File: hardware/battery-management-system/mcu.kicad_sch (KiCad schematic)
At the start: 32 parts, among them J6 ARM-JTAG-SWD, Q5 DMN3404L, Q6 DMN3404L, Q7 DMN3404L, U7 STM32L071CZTx, U8 AT24C512C, U9 NCT75DR2G

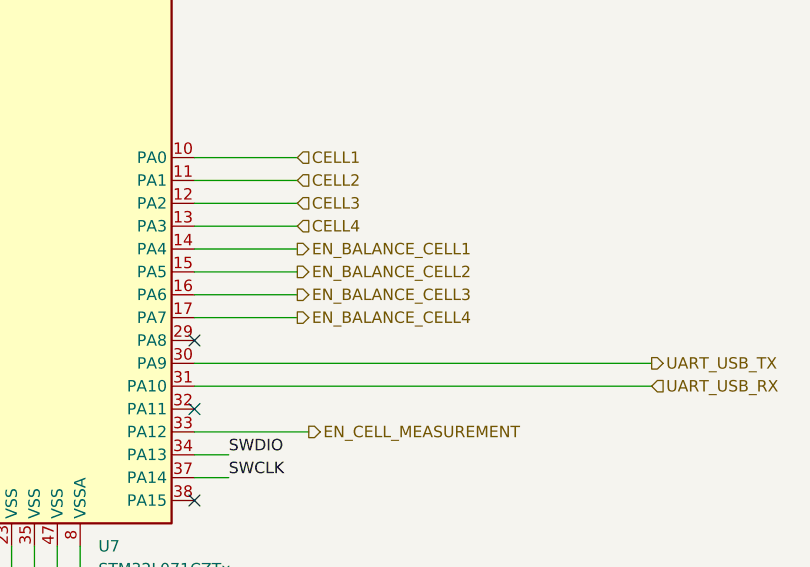
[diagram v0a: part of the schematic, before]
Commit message: finish layout of BMS
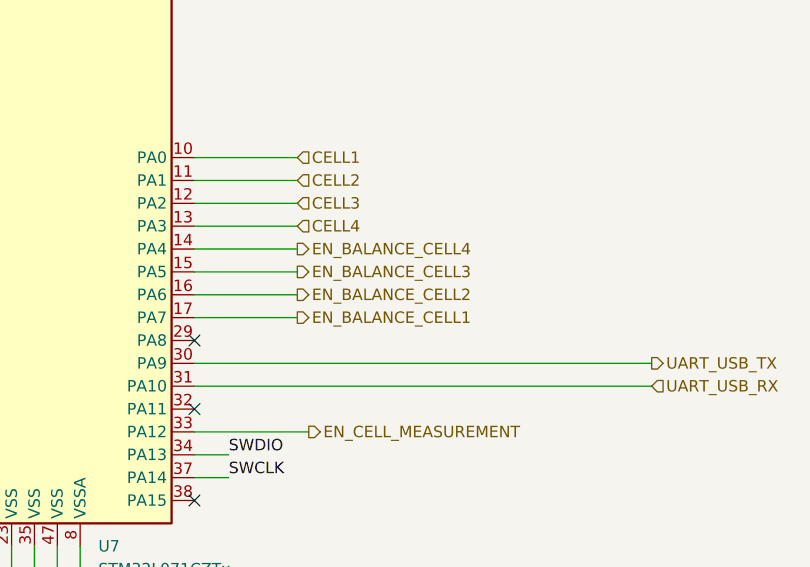
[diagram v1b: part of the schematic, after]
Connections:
- net EN_BALANCE_CELL1: now also U7.17 (PA7); no longer U7.14 (PA4)
- net EN_BALANCE_CELL2: now also U7.16 (PA6); no longer U7.15 (PA5)
- net EN_BALANCE_CELL3: now also U7.15 (PA5); no longer U7.16 (PA6)
- net EN_BALANCE_CELL4: now also U7.14 (PA4); no longer U7.17 (PA7)

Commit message: update symbols from library
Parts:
- C22: Mouser Part Number (none) -> 187-CL31A106MBHNNNE
- C23, C24, C25, C26, C27, C29, C30, C31: Mouser Part Number (none) -> 581-KGM15BR71H104KM
- C28: Mouser Part Number (none) -> 963-UMK107BJ105KA-T
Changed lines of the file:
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@@
 			)
 		)
+		(property "Mouser Part Number" "963-UMK107BJ105KA-T"
+			(at 147.066 39.37 0)
+			(effects
+				(font
+					(size 1.27 1.27)
+				)
+				(hide yes)
+			)
+		)
 		(pin "1"
 		)
@@
 			)
 		)
+		(property "Mouser Part Number" "581-KGM15BR71H104KM"
+			(at 114.046 88.9 0)
+			(effects
+				(font
+					(size 1.27 1.27)
+				)
+				(hide yes)
+			)
+		)
 		(pin "1"
 		)
@@
 			)
 		)
+		(property "Mouser Part Number" "581-KGM15BR71H104KM"
+			(at 82.296 39.37 0)
+			(effects
+				(font
+					(size 1.27 1.27)
+				)
+				(hide yes)
+			)
+		)
 		(pin "1"
 		)
@@
 			)
 		)
+		(property "Mouser Part Number" "581-KGM15BR71H104KM"
+			(at 107.696 39.37 0)
+			(effects
+				(font
+					(size 1.27 1.27)
+				)
+				(hide yes)
+			)
+		)
 		(pin "1"
 		)
@@
 			)
 		)
+		(property "Mouser Part Number" "581-KGM15BR71H104KM"
+			(at 94.996 39.37 0)
+			(effects
+				(font
+					(size 1.27 1.27)
+				)
+				(hide yes)
+			)
+		)
 		(pin "1"
 		)
@@
 			)
 		)
+		(property "Mouser Part Number" "581-KGM15BR71H104KM"
+			(at 134.366 39.37 0)
+			(effects
+				(font
+					(size 1.27 1.27)
+				)
+				(hide yes)
+			)
+		)
 		(pin "1"
 		)
@@
 			)
 		)
+		(property "Mouser Part Number" "581-KGM15BR71H104KM"
+			(at 92.456 121.92 0)
+			(effects
+				(font
+					(size 1.27 1.27)
+				)
+				(hide yes)
+			)
+		)
 		(pin "1"
 		)
@@
 			)
 		)
+		(property "Mouser Part Number" "581-KGM15BR71H104KM"
+			(at 48.006 120.65 0)
+			(effects
+				(font
+					(size 1.27 1.27)
+				)
+				(hide yes)
+			)
+		)
 		(pin "1"
 		)
@@
 			)
 		)
+		(property "Mouser Part Number" "187-CL31A106MBHNNNE"
+			(at 70.866 39.37 0)
+			(effects
+				(font
+					(size 1.27 1.27)
+				)
+				(hide yes)
+			)
+		)
 		(pin "1"
 		)
@@
 			(at 120.396 39.37 0)
 			(effects
+				(font
+					(size 1.27 1.27)
+				)
+				(hide yes)
+			)
+		)
+		(property "Mouser Part Number" "581-KGM15BR71H104KM"
+			(at 120.396 39.37 0)
+			(effects

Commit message: update symbols from library
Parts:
- R23, R24, R30, R31, R32: Mouser Part Number (none) -> 652-CR0603FX-1002ELF
- R25, R26: Mouser Part Number (none) -> 652-CR0603FX-4701ELF
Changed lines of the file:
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@@
+			)
+		)
+		(property "Mouser Part Number" "652-CR0603FX-1002ELF"
+			(at 99.06 168.91 0)
+			(effects
+				(font
+					(size 1.27 1.27)
+				)
+				(hide yes)
 			)
 		)
@@
 			)
 		)
+		(property "Mouser Part Number" "652-CR0603FX-1002ELF"
+			(at 176.53 60.96 0)
+			(effects
+				(font
+					(size 1.27 1.27)
+				)
+				(hide yes)
+			)
+		)
 		(pin "1"
 		)
@@
 			)
 		)
+		(property "Mouser Part Number" "652-CR0603FX-4701ELF"
+			(at 118.11 73.66 0)
+			(effects
+				(font
+					(size 1.27 1.27)
+				)
+				(hide yes)
+			)
+		)
 		(pin "1"
 		)
@@
 			)
 		)
+		(property "Mouser Part Number" "652-CR0603FX-1002ELF"
+			(at 63.5 168.91 0)
+			(effects
+				(font
+					(size 1.27 1.27)
+				)
+				(hide yes)
+			)
+		)
 		(pin "1"
 		)
@@
 			)
 		)
+		(property "Mouser Part Number" "652-CR0603FX-1002ELF"
+			(at 26.67 168.91 0)
+			(effects
+				(font
+					(size 1.27 1.27)
+				)
+				(hide yes)
+			)
+		)
 		(pin "1"
 		)
@@
 		)
 		(property "RS order number" "901-3581"
+			(at 130.81 73.66 0)
+			(effects
+				(font
+					(size 1.27 1.27)
+				)
+				(hide yes)
+			)
+		)
+		(property "Mouser Part Number" "652-CR0603FX-4701ELF"
 			(at 130.81 73.66 0)
 			(effects
@@
 			(at 62.23 68.58 0)
 			(effects
+				(font
+					(size 1.27 1.27)
+				)
+				(hide yes)
+			)
+		)
+		(property "Mouser Part Number" "652-CR0603FX-1002ELF"
+			(at 62.23 68.58 0)
+			(effects

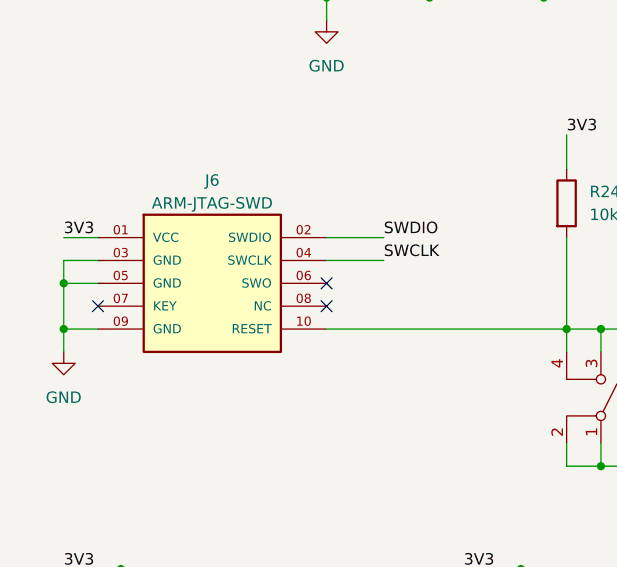
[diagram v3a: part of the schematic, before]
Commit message: update symbols from library
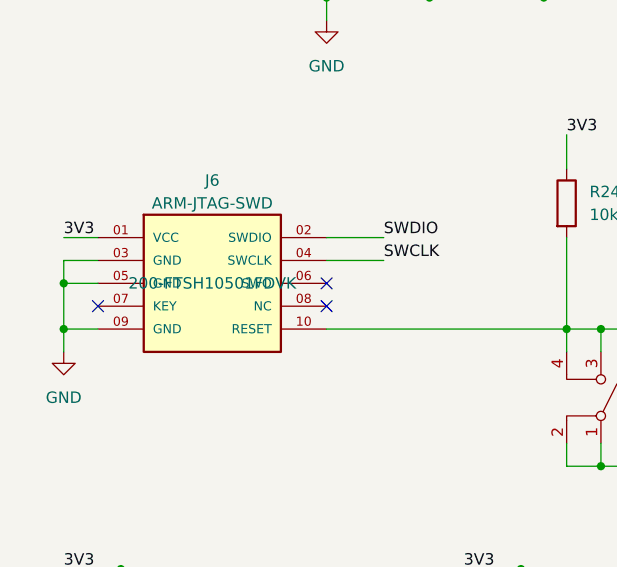
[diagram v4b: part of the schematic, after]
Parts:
- D14: Mouser Part Number (none) -> 604-AP1608SGC
- D15: Mouser Part Number (none) -> 604-APH1608SURCK
- D16: Mouser Part Number (none) -> 604-APG1608SYKC/T
- FB2: Mouser Part Number (none) -> 81-BLM11P300S
- J6: Mouser Part Number (none) -> 200-FTSH10501FDVK
- Q5, Q6, Q7: Mouser Part Number (none) -> 621-DMN3404L-7
- R27, R28, R29: Mouser Part Number (none) -> 279-CRGH0603F100R
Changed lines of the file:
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@@
 			)
 		)
+		(property "Mouser Part Number" "279-CRGH0603F100R"
+			(at 19.05 167.64 0)
+			(effects
+				(font
+					(size 1.27 1.27)
+				)
+				(hide yes)
+			)
+		)
 		(pin "1"
 		)
@@
 			)
 		)
+		(property "Mouser Part Number" "621-DMN3404L-7"
+			(at 31.75 185.42 0)
+			(effects
+				(font
+					(size 1.27 1.27)
+				)
+				(hide yes)
+			)
+		)
 		(pin "1"
 		)
@@
 			)
 		)
+		(property "Mouser Part Number" "604-APG1608SYKC/T"
+			(at 109.22 158.75 0)
+			(effects
+				(font
+					(size 1.27 1.27)
+				)
+				(hide yes)
+			)
+		)
 		(pin "1"
 		)
@@
 			)
 		)
+		(property "Mouser Part Number" "621-DMN3404L-7"
+			(at 104.14 185.42 0)
+			(effects
+				(font
+					(size 1.27 1.27)
+				)
+				(hide yes)
+			)
+		)
 		(pin "1"
 		)
@@
 			)
 		)
+		(property "Mouser Part Number" "279-CRGH0603F100R"
+			(at 55.88 167.64 0)
+			(effects
+				(font
+					(size 1.27 1.27)
+				)
+				(hide yes)
+			)
+		)
 		(pin "1"
 		)
@@
 			)
 		)
+		(property "Mouser Part Number" "621-DMN3404L-7"
+			(at 68.58 185.42 0)
+			(effects
+				(font
+					(size 1.27 1.27)
+				)
+				(hide yes)
+			)
+		)
 		(pin "1"
 		)
@@
 			)
 		)
+		(property "Mouser Part Number" "604-APH1608SURCK"
+			(at 73.66 158.75 0)
+			(effects
+				(font
+					(size 1.27 1.27)
+				)
+				(hide yes)
+			)
+		)
 		(pin "1"
 		)
@@
 			)
 		)
+		(property "Mouser Part Number" "604-AP1608SGC"
+			(at 36.83 158.75 0)
+			(effects
+				(font
+					(size 1.27 1.27)
+				)
+				(hide yes)
+			)
+		)
 		(pin "1"
 		)
@@
 			)
 		)
+		(property "Mouser Part Number" "200-FTSH10501FDVK"
+			(at 40.64 78.74 0)
+			(effects
+				(font
+					(size 1.27 1.27)
+				)
+			)
+		)
 		(pin "10"
 		)
@@
 			)
 		)
+		(property "Mouser Part Number" "279-CRGH0603F100R"
+			(at 91.44 167.64 0)
+			(effects
+				(font
+					(size 1.27 1.27)
+				)
+				(hide yes)
+			)
+		)
 		(pin "1"
 		)
@@
 			(at 110.49 31.75 0)
 			(effects
+				(font
+					(size 1.27 1.27)
+				)
+				(hide yes)
+			)
+		)
+		(property "Mouser Part Number" "81-BLM11P300S"
+			(at 110.49 31.75 0)
+			(effects

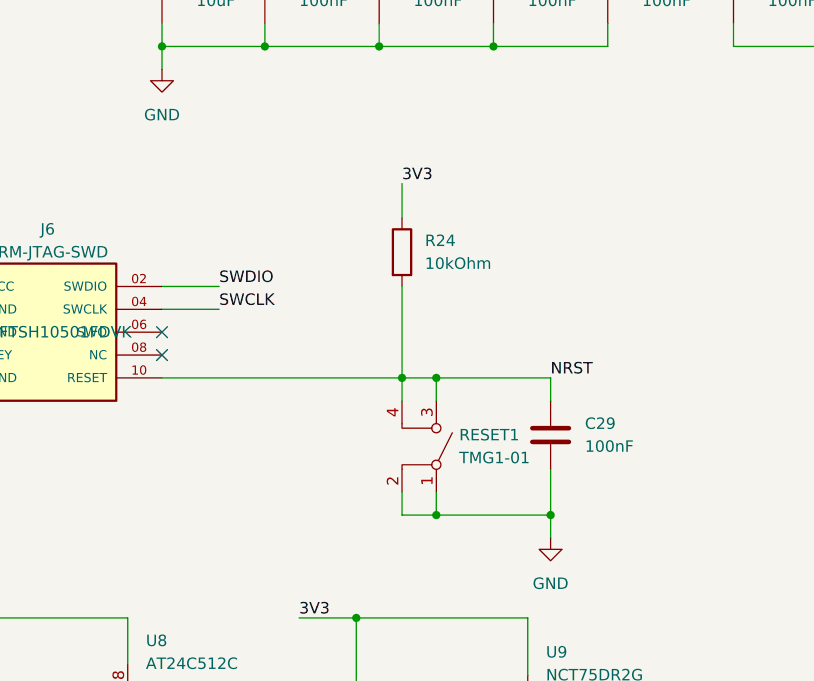
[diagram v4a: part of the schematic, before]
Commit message: replace reset button, update symbols
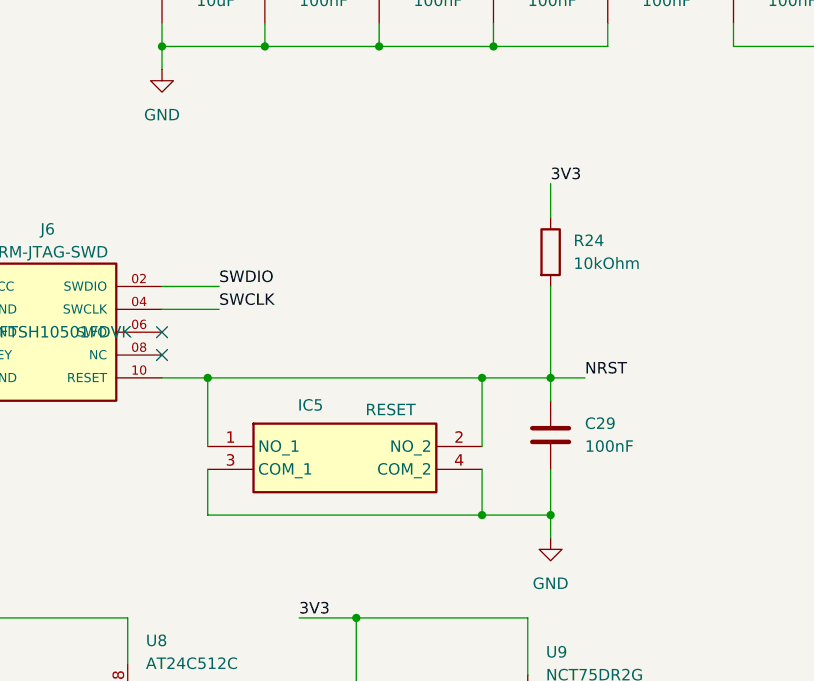
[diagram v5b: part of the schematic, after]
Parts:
- removed RESET1: TMG1-01, benediktibk:TMG1-01, symbol benediktibk:TMG1-01
- added IC5: RESET, benediktibk:TS026650BK100SCRD, symbol benediktibk:TS02-66-50-BK-100-SCR-D
- U7: Mouser Part Number (none) -> 511-STM32L071CZT6
- U8: Mouser Part Number (none) -> 556-AT24C512C-SSHM-T
- U9: Mouser Part Number (none) -> 863-NCT75DR2G
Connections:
- net GND: now also IC5.3 (COM_1), IC5.4 (COM_2)
- net NRST: now also IC5.1 (NO_1), IC5.2 (NO_2)
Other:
- moved on the sheet: R24

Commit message: update symbols and BOM
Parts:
- D15: Mouser Part Number 604-APH1608SURCK -> 859-LTST-C190KDKT10A
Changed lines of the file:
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@@
 			)
 		)
-		(property "Mouser Part Number" "604-APH1608SURCK"
+		(property "Mouser Part Number" "859-LTST-C190KDKT10A"
 			(at 73.66 158.75 0)
 			(effects
